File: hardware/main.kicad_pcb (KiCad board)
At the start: 6 copper layers, 57 x 92 mm, 430 parts, among them J1 DS1128-09-S8B8X, J10 AS0BC21-S30BM-7H, J2 DS1128-09-S8B8X, J3 DS1128-09-S8B8X, J4 98424-G52-04ALF, J5 miniPCI-E_52P_5.2, J6 1042240820, J8 USB_C_Receptacle, J9 TYPE-C-31-M-12, Q1 SSM6J501NU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

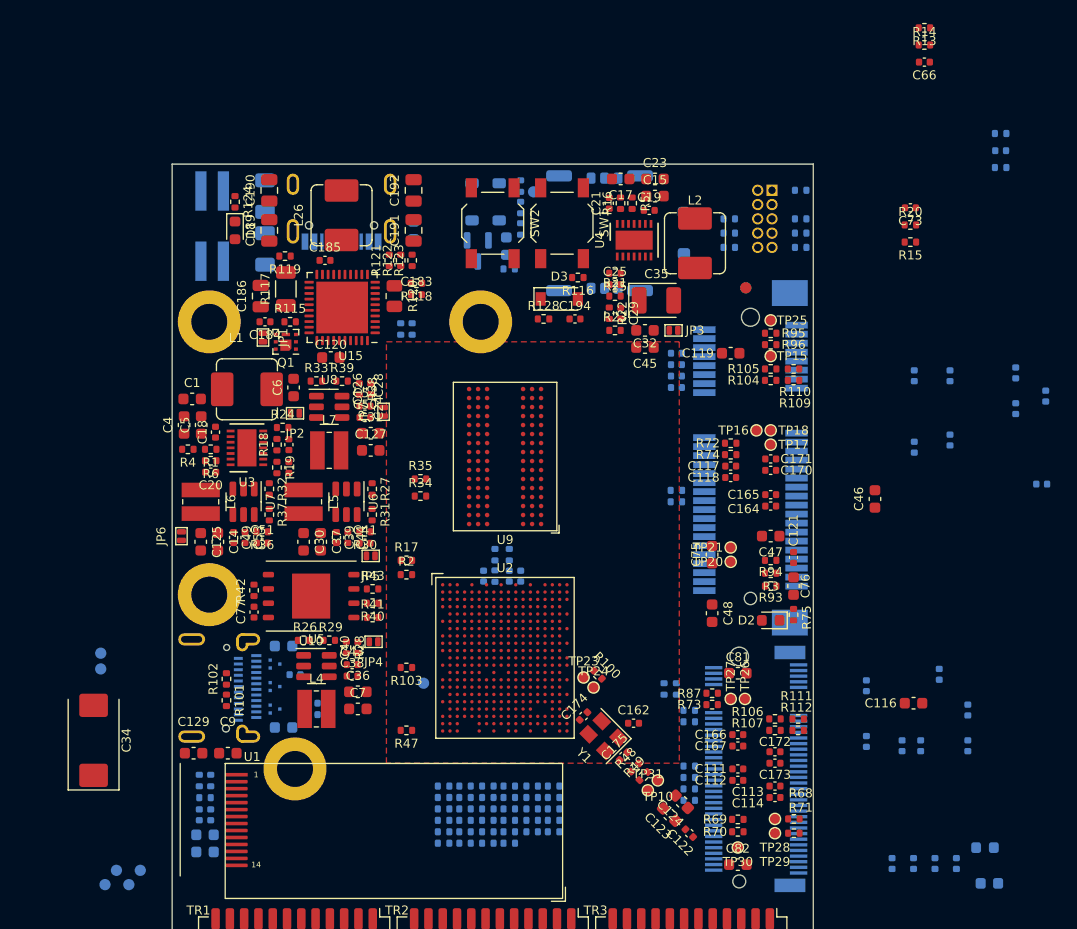
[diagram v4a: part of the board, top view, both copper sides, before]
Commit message: update pin layout
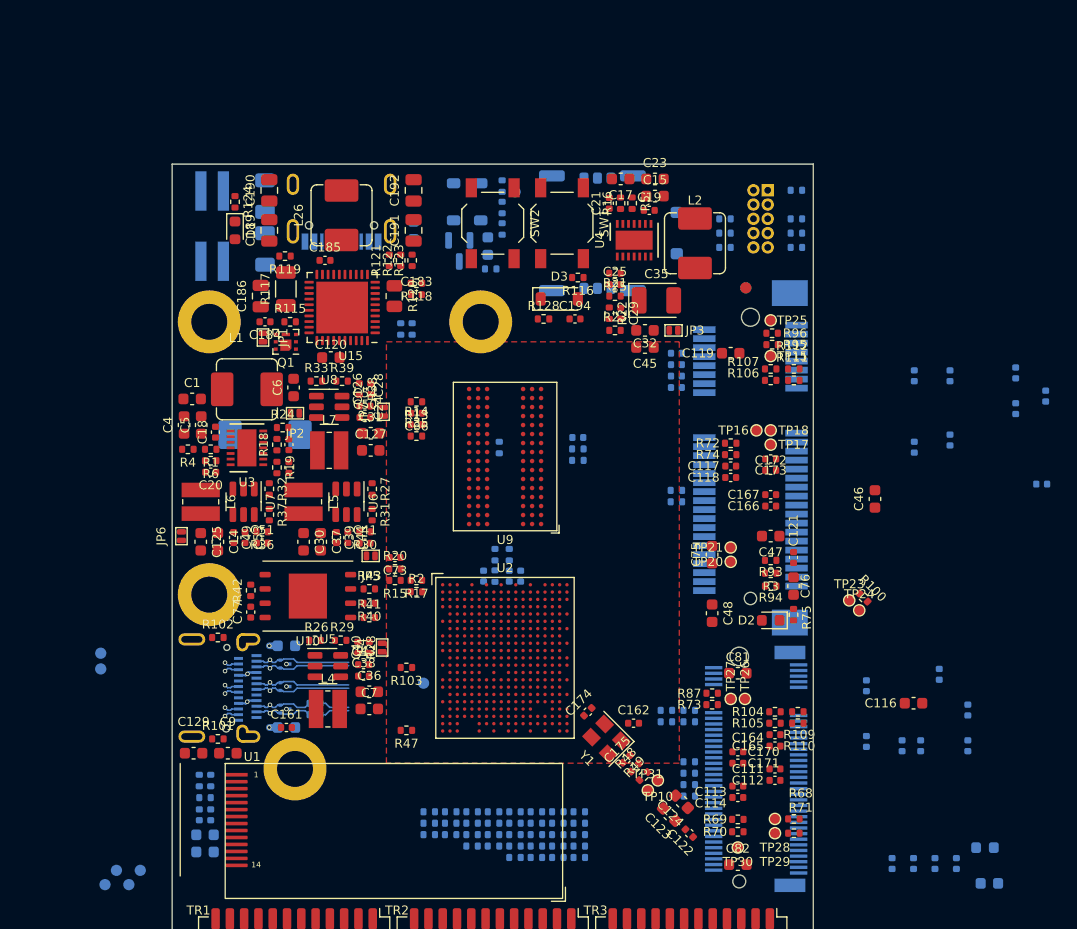
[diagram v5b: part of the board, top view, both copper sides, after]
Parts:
- C161: moved to F.Cu
- C34, R34: moved to B.Cu
- moved R14 56.4 mm to (21.7, -68.8)
- moved R13 56.1 mm to (21.7, -70.9)
- moved C73 55.4 mm to (19.8, -57.0)
- moved R20 55.1 mm to (19.8, -56.0)
- moved C66 54.9 mm to (21.7, -69.8)
- moved R15 54.8 mm to (19.8, -55.0)
- moved R11 46.9 mm to (36.1, -66.7), turned to 180 degrees
- moved R10 45.7 mm to (36.1, -65.7), turned to 0 degrees
- moved C59 45.4 mm to (36.1, -67.7), turned to 0 degrees
- moved R107 32.1 mm to (53.2, -73.8)
- moved R112 32.1 mm to (55.3, -73.8)
- moved R105 31.5 mm to (53.6, -42.3)
- moved R110 31.5 mm to (55.6, -42.3)
- moved C34 31.2 mm to (8.26, -67.9), turned to 180 degrees
- moved R106 30.1 mm to (53.2, -72.8)
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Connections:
- net /RTS2_N renamed /_UART1_RTS
- net /RTS3_N renamed /_UART3_RTS
- net /TXD1 renamed /_UART0_TXD
- net /TXD2 renamed /_UART1_TXD
- net Net-(U2B-CTS2_N) renamed /_UART1_CTS
- net Net-(U2B-CTS3_N) renamed /_UART3_CTS
- net Net-(U2B-RXD1) renamed /_UART0_RXD
- net Net-(U2B-RXD2) renamed /_UART1_RXD
- net Net-(U2B-RXD3) renamed /_UART3_RXD
- net Net-(U2B-TXD3) renamed /_UART3_TXD
- J10 pad 32: /UART3_CTS -> /UART3_TXD
- J10 pad 36: /UART3_TXD -> /UART3_CTS
- J10 pad 41: /PCIE_RX1_N -> /PCIE_RX0_N
- J10 pad 43: /PCIE_RX1_P -> /PCIE_RX0_P
- J10 pad 47: /PCIE_TX1_N -> /PCIE_TX0_N
- J10 pad 49: /PCIE_TX1_P -> /PCIE_TX0_P
- J10 pad 53: /PCIE_CK1_N -> /PCIE_CK0_N
- J10 pad 55: /PCIE_CK1_P -> /PCIE_CK0_P
- J5 pad 11: /PCIE_CK0_N -> /PCIE_CK1_N
- J5 pad 13: /PCIE_CK0_P -> /PCIE_CK1_P
- J5 pad 23: /PCIE_RX0_N -> /PCIE_RX1_N
- J5 pad 25: /PCIE_RX0_P -> /PCIE_RX1_P
- J5 pad 3: /UART1_CTS -> /UART1_RTS
- J5 pad 31: /PCIE_TX0_N -> /PCIE_TX1_N
- J5 pad 33: /PCIE_TX0_P -> /PCIE_TX1_P
- J5 pad 45: /UART1_RXD -> /UART1_TXD
- J5 pad 5: /UART1_RTS -> /UART1_CTS
- J5 pad 51: /UART1_TXD -> /UART1_RXD
- R82 pad 2: Net-(J10-NC-Pad58) -> Net-(J10-NC-Pad56)
- R83 pad 1: Net-(J10-NC-Pad56) -> Net-(J10-NC-Pad58)
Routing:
- net /USB_RXN: track 0.00 -> 10.0 mm, vias 0 -> 2
- net /USB_DP: track 0.00 -> 10.0 mm, vias 0 -> 2
- net /USB_RXP: track 0.00 -> 10.0 mm, vias 0 -> 2
- net /USB_DN: track 0.00 -> 10.0 mm, vias 0 -> 2
- net /_USB_TXN: track 0.00 -> 6.70 mm, vias 0 -> 2
- net /_USB_TXP: track 0.00 -> 6.70 mm, vias 0 -> 2
- net +5V: track 0.00 -> 4.93 mm, vias 0 -> 4
- net /USB_TXP: track 0.00 -> 2.67 mm
- net /USB_TXN: track 0.00 -> 2.67 mm
- net -BATT: track 0.00 -> 0.88 mm, vias 0 -> 3

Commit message: update silk
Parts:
- R100: moved to B.Cu
- moved TP11 96.3 mm to (70.4, -24.1)
- moved TP32 96.3 mm to (92.3, -22.4)
- moved TP33 96.3 mm to (91.2, -23.6)
- moved TP12 96.3 mm to (72.9, -24.1)
- moved TP13 96.3 mm to (71.6, -22.9)
- moved TP14 96.3 mm to (71.6, -24.1)
- moved TP22 96.3 mm to (90.2, -22.4)
- moved TP34 96.3 mm to (93.3, -23.6)
- moved TP4 96.3 mm to (77.6, -36.6)
- moved TP5 96.3 mm to (79.4, -35.9)
- moved TP6 96.3 mm to (76.5, -36.1)
- moved TP7 96.3 mm to (78.2, -35.6)
- moved TP8 96.3 mm to (77.1, -35.1)
- moved TP9 96.3 mm to (78.7, -37.0)
- moved TP1 85.1 mm to (78.6, -41.9)
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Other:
- outline, holes or cut-outs redrawn
- board text added: "OPR"
- board text added: "Open Pocket Router"
- board text added: "rev 0.6"
